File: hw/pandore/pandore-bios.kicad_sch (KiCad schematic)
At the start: 11 parts, among them U2 mem_flash_spi

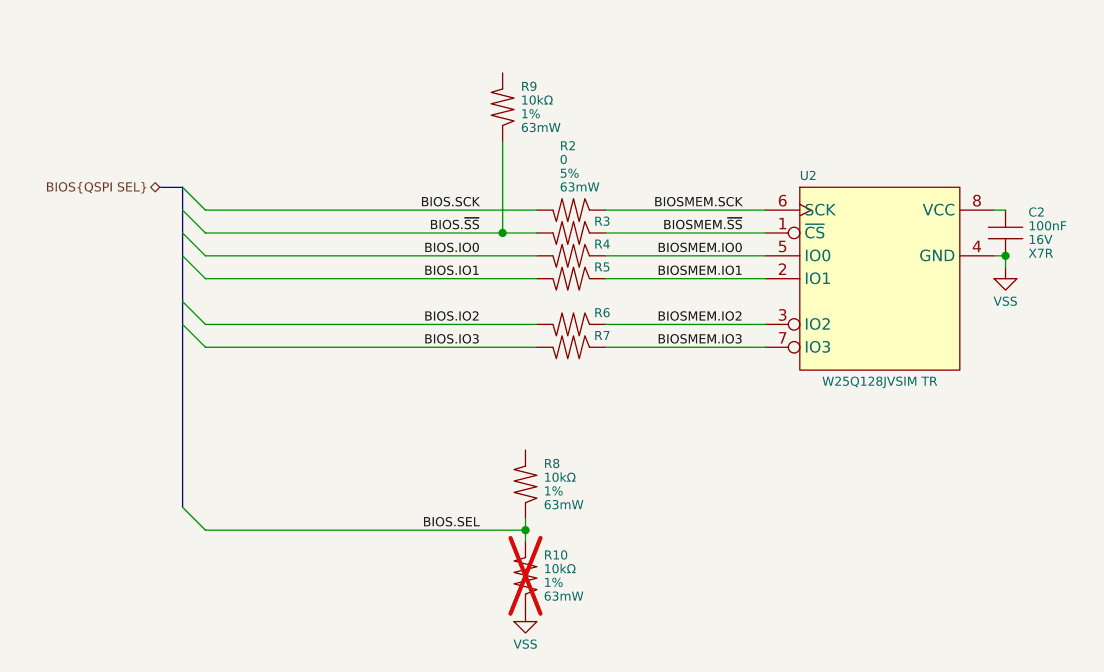
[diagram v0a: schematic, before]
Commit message: lcd control circuit added fan interface added rgba output pinout for management mcu accessories done
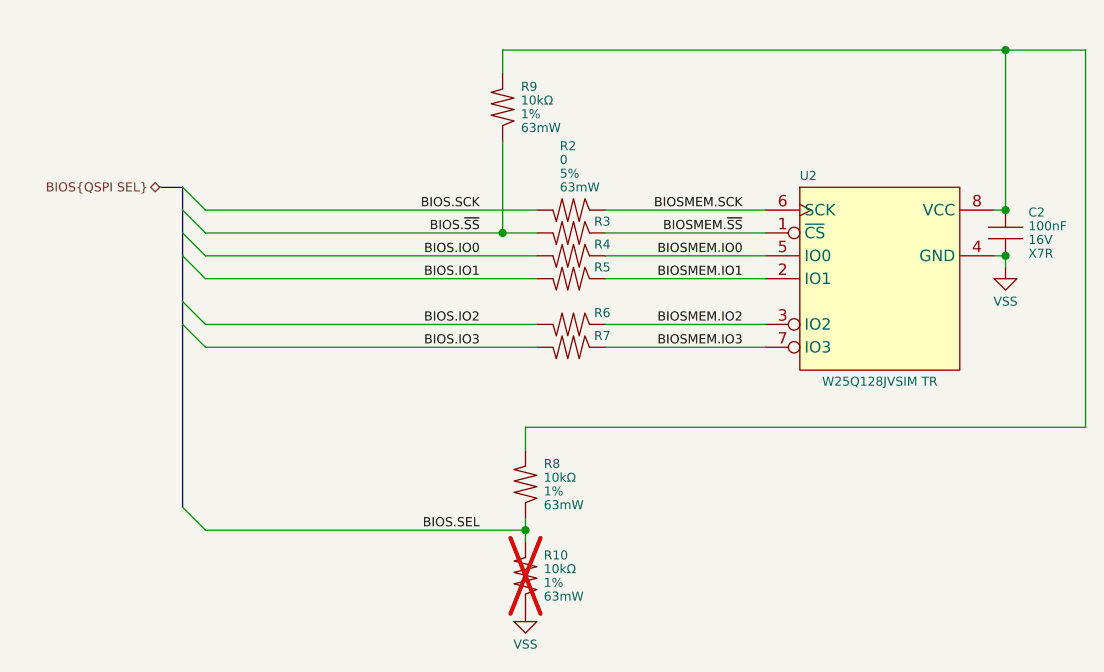
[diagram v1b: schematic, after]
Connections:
- net at R8.1: now also C2.2, R9.1, U2.8 (VCC)
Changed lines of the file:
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@@
+	)
+	(junction
+		(at 130.81 50.8)
+		(diameter 0)
+		(color 0 0 0 0)
+	)
+	(junction
+		(at 130.81 68.58)
+		(diameter 0)
+		(color 0 0 0 0)
 	)
 	(junction
@@
 		)
 	)
+	(wire
+		(pts
+			(xy 74.93 50.8) (xy 130.81 50.8)
+		)
+		(stroke
+			(width 0)
+			(type default)
+		)
+	)
 	(bus
 		(pts
@@
 	(wire
 		(pts
+			(xy 139.7 92.71) (xy 139.7 50.8)
+		)
+		(stroke
+			(width 0)
+			(type default)
+		)
+	)
+	(wire
+		(pts
+			(xy 74.93 53.34) (xy 74.93 50.8)
+		)
+		(stroke
+			(width 0)
+			(type default)
+		)
+	)
+	(wire
+		(pts
 			(xy 41.91 68.58) (xy 78.74 68.58)
 		)
@@
 		)
 	)
+	(wire
+		(pts
+			(xy 139.7 50.8) (xy 130.81 50.8)
+		)
+		(stroke
+			(width 0)
+			(type default)
+		)
+	)
 	(bus
 		(pts
@@
 	(wire
 		(pts
+			(xy 77.47 92.71) (xy 139.7 92.71)
+		)
+		(stroke
+			(width 0)
+			(type default)
+		)
+	)
+	(wire
+		(pts
 			(xy 86.36 83.82) (xy 104.14 83.82)
 		)
@@
 	(wire
 		(pts
+			(xy 77.47 95.25) (xy 77.47 92.71)
+		)
+		(stroke
+			(width 0)
+			(type default)
+		)
+	)
+	(wire
+		(pts
 			(xy 86.36 68.58) (xy 104.14 68.58)
 		)
@@
 		)
 		(stroke
+			(width 0)
+			(type default)
+		)
+	)
+	(wire
+		(pts
+			(xy 130.81 50.8) (xy 130.81 68.58)
+		)
+		(stroke

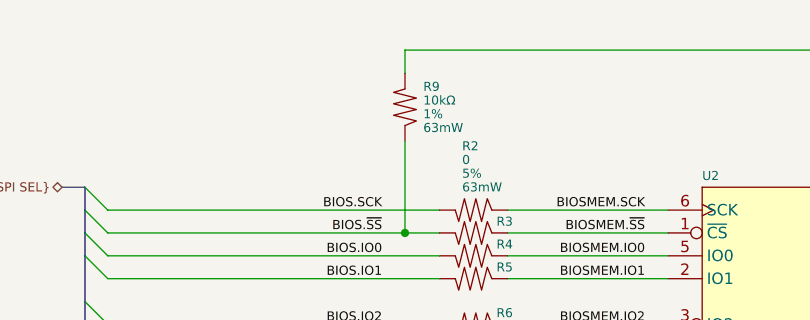
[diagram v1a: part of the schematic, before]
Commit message: most of board control signals added, routed and defined
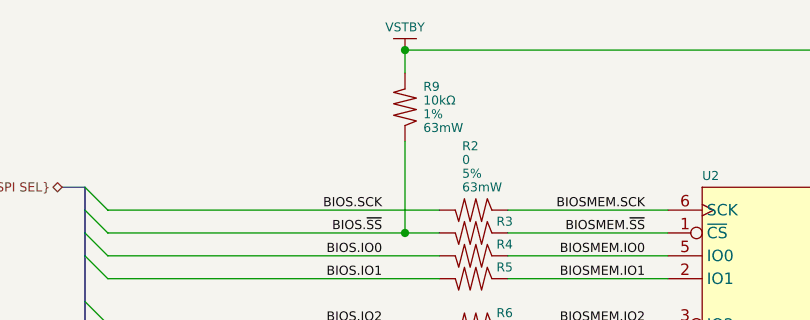
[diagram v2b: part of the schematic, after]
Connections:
- net VSTBY: now reaches C2.2, R8.1, R9.1, U2.8 (VCC)
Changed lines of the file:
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@@
+	)
+	(junction
+		(at 74.93 50.8)
+		(diameter 0)
+		(color 0 0 0 0)
 	)
 	(junction
@@
 				)
 			)
+		)
+	)
+	(symbol
+		(lib_id "megaxone_power:VSTBY")
+		(at 74.93 49.53 0)
+		(unit 1)
+		(exclude_from_sim no)
+		(in_bom yes)
+		(on_board yes)
+		(dnp no)
+		(property "Reference" "#PWR0314"
+			(at 74.93 52.07 0)
+			(effects
+				(font
+					(size 1.524 1.524)
+				)
+				(hide yes)
+			)
+		)
+		(property "Value" "VSTBY"
+			(at 74.93 48.26 0)
+			(effects
+				(font
+					(size 0.9906 0.9906)
+				)
+			)
+		)
+		(property "Footprint" ""
+			(at 74.93 49.53 0)
+			(effects
+				(font
+					(size 1.524 1.524)
+				)
+			)
+		)
+		(property "Datasheet" ""
+			(at 74.93 49.53 0)
+			(effects
+				(font
+					(size 1.524 1.524)
+				)
+			)
+		)
+		(property "Description" ""
+			(at 74.93 49.53 0)
+			(effects
+				(font
+					(size 1.27 1.27)
+				)
+				(hide yes)
+			)
+		)
+		(pin "1"
+		)
+		(instances
+			(project "pandore"
+				(path "/e55f2700-f75a-4062-8a27-fe258faa8966/88bddcf3-091d-4999-8622-d323c703fd74/b0d5502d-1c9e-460a-aaa4-6a1fd0bb26fe"
+					(reference "#PWR0314")
+					(unit 1)
+				)
+			)

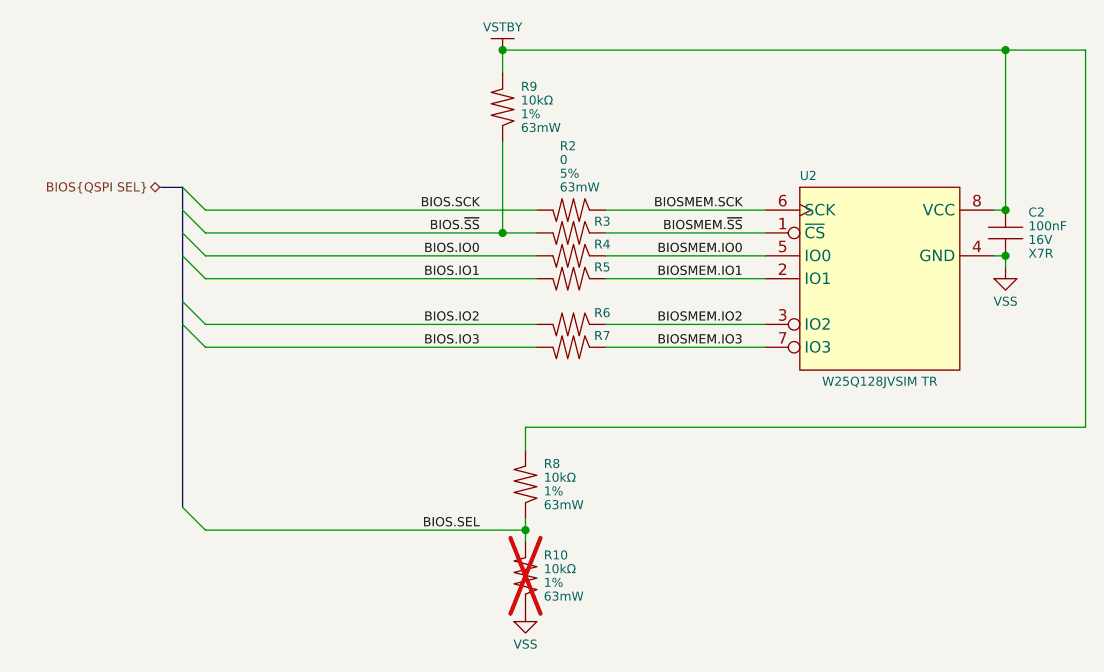
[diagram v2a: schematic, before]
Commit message: finished adding mpn,mfg to all parts, finished routing placement
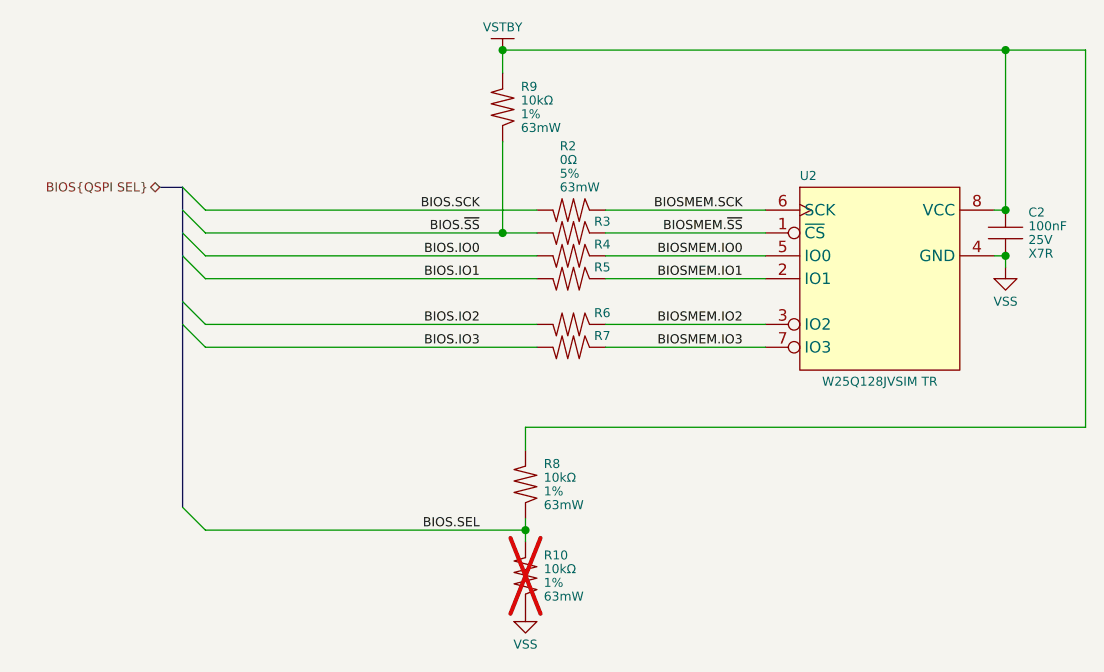
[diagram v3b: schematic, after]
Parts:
- C2: MFG2 Samsung Electro-Mechanics -> (none); MFG3 Taiyo Yuden -> (none); MPN2 CL05B104KA5NNNC -> (none); MPN3 EMK105B7104KV-F -> (none); Voltage 16V -> 25V
- R2, R3, R4, R5, R6, R7: Resistance 0 -> 0Ω
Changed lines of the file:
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@@
 			)
 		)
-		(property "Resistance" "0"
+		(property "Resistance" "0Ω"
 			(at 81.28 62.992 90)
 			(do_not_autoplace yes)
@@
 			)
 		)
-		(property "Resistance" "0"
+		(property "Resistance" "0Ω"
 			(at 81.28 70.612 90)
 			(do_not_autoplace yes)
@@
 			)
 		)
-		(property "Voltage" "16V"
+		(property "Voltage" "25V"
 			(at 133.35 71.882 0)
 			(do_not_autoplace yes)
@@
 			)
 		)
-		(property "MPN2" "CL05B104KA5NNNC"
+		(property "MPN2" ""
 			(at 130.81 91.44 0)
 			(do_not_autoplace yes)
@@
 			)
 		)
-		(property "MFG2" "Samsung Electro-Mechanics"
+		(property "MFG2" ""
 			(at 142.748 91.44 0)
 			(do_not_autoplace yes)
@@
 			)
 		)
-		(property "MPN3" "EMK105B7104KV-F"
+		(property "MPN3" ""
 			(at 130.81 92.964 0)
 			(do_not_autoplace yes)
@@
 			)
 		)
-		(property "MFG3" "Taiyo Yuden"
+		(property "MFG3" ""
 			(at 142.748 92.964 0)
 			(do_not_autoplace yes)
@@
 			)
 		)
-		(property "Resistance" "0"
+		(property "Resistance" "0Ω"
 			(at 81.28 78.232 90)
 			(do_not_autoplace yes)
@@
 			)
 		)
-		(property "Resistance" "0"
+		(property "Resistance" "0Ω"
 			(at 81.28 75.692 90)
 			(do_not_autoplace yes)
@@
 			)
 		)
-		(property "Resistance" "0"
+		(property "Resistance" "0Ω"
 			(at 81.28 68.072 90)
 			(do_not_autoplace yes)
@@
 			)
 		)
-		(property "Resistance" "0"
+		(property "Resistance" "0Ω"
 			(at 81.28 65.532 90)
 			(do_not_autoplace yes)
